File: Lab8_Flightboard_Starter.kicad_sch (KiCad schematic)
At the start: 64 parts, among them J1 Motor1, J10 ESC3_GND, J11 ESC4_VBAT, J12 ESC4_GND, J2 Motor2, J3 Motor3, J4 Motor4, J5 ESC1_VBAT, J6 ESC1_GND, J7 ESC2_VBAT, J8 ESC2_GND, J9 ESC3_VBAT, Q1 DMP6023LE-13, U1 Teensy4.0, U2 TPS62933, U4 LP5912-3.3DRV, U5 LP5912-3.3DRV, U6 NRF24L01_Breakout, U9 LSM6DSO32_Adafruit

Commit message: Fixed more ground nodes
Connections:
- net GND: no longer U1.47 (GND)
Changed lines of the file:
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@@
 	(wire
 		(pts
-			(xy 52.07 133.35) (xy 54.61 133.35)
-		)
-		(stroke
-			(width 0)
-			(type default)
-		)
-	)
-	(wire
-		(pts
 			(xy 143.51 44.45) (xy 147.32 44.45)
 		)
@@
 	(wire
 		(pts
-			(xy 110.49 151.13) (xy 114.3 151.13)
-		)
-		(stroke
-			(width 0)
-			(type default)
-		)
-	)
-	(wire
-		(pts
 			(xy 78.74 53.34) (xy 78.74 52.07)
 		)
@@
 		)
 	)
-	(wire
-		(pts
-			(xy 50.8 173.99) (xy 54.61 173.99)
-		)
-		(stroke
-			(width 0)
-			(type default)
-		)
-	)
 	(polyline
 		(pts
@@
 		)
 	)
-	(label "GND"
-		(at 114.3 151.13 0)
-		(effects
-			(font
-				(size 0.889 0.889)
-			)
-			(justify left bottom)
-		)
-	)
 	(label "SCK"
 		(at 342.9 44.45 180)
@@
 		)
 	)
-	(label "GND"
-		(at 52.07 133.35 180)
-		(effects
-			(font
-				(size 0.889 0.889)
-			)
-			(justify right bottom)
-		)
-	)
-	(label "GND"
-		(at 50.8 173.99 180)
-		(effects
-			(font
-				(size 0.889 0.889)
-			)
-			(justify right bottom)
-		)
-	)
 	(label "CS"
 		(at 278.13 104.14 180)
@@
 	)
 	(symbol
+		(lib_id "power:GND")
+		(at 54.61 173.99 270)
+		(unit 1)
+		(body_style 1)
+		(exclude_from_sim no)
+		(in_bom yes)
+		(on_board yes)
+		(in_pos_files yes)
+		(dnp no)
+		(fields_autoplaced yes)
+		(property "Reference" "#PWR043"
+			(at 48.26 173.99 0)
+			(hide yes)
+			(show_name no)
+			(do_not_autoplace no)
+			(effects
+				(font
+					(size 1.27 1.27)
+				)
+			)
+		)
+		(property "Value" "GND"
+			(at 50.8 173.9899 90)
+			(show_name no)
+			(do_not_autoplace no)
+			(effects
+				(font
+					(size 1.27 1.27)
+				)
+				(justify right)
+			)
+		)
+		(property "Footprint" ""
+			(at 54.61 173.99 0)
+			(hide yes)
+			(show_name no)
+			(do_not_autoplace no)
+			(effects
+				(font
+					(size 1.27 1.27)
+				)
+			)
+		)
+		(property "Datasheet" ""
+			(at 54.61 173.99 0)
+			(hide yes)
+			(show_name no)
+			(do_not_autoplace no)
+			(effects
+				(font
+					(size 1.27 1.27)
+				)
+			)
+		)
+		(property "Description" "Power symbol creates a global label with name \"GND\" , ground"
+			(at 54.61 173.99 0)
+			(hide yes)
+			(show_name no)
+			(do_not_autoplace no)
+			(effects
+				(font
+					(size 1.27 1.27)
+				)
+			)
+		)
+		(pin "1"
+		)
+		(instances
+			(project "Lab8_Flightboard_Starter"
+				(path "/8da9c326-3337-46e2-8624-067ffceed853"
+					(reference "#PWR043")
+					(unit 1)
+				)
+			)
+		)
+	)
+	(symbol
 		(lib_id "IMU_Symbols:LSM6DSO32_Adafruit")
 		(at 293.37 106.68 0)
@@
 	)
 	(symbol
+		(lib_id "power:GND")
+		(at 54.61 133.35 270)
+		(unit 1)
+		(body_style 1)
+		(exclude_from_sim no)
+		(in_bom yes)
+		(on_board yes)
+		(in_pos_files yes)
+		(dnp no)
+		(fields_autoplaced yes)
+		(property "Reference" "#PWR044"
+			(at 48.26 133.35 0)
+			(hide yes)
+			(show_name no)
+			(do_not_autoplace no)
+			(effects
+				(font
+					(size 1.27 1.27)
+				)
+			)
+		)
+		(property "Value" "GND"
+			(at 50.8 133.3499 90)
+			(show_name no)
+			(do_not_autoplace no)
+			(effects
+				(font
+					(size 1.27 1.27)
+				)
+				(justify right)
+			)
+		)
+		(property "Footprint" ""
+			(at 54.61 133.35 0)
+			(hide yes)
+			(show_name no)
+			(do_not_autoplace no)
+			(effects
+				(font
+					(size 1.27 1.27)
+				)
+			)
+		)
+		(property "Datasheet" ""
+			(at 54.61 133.35 0)
+			(hide yes)
+			(show_name no)
+			(do_not_autoplace no)
+			(effects
+				(font
+					(size 1.27 1.27)
+				)
+			)
+		)
+		(property "Description" "Power symbol creates a global label with name \"GND\" , ground"
+			(at 54.61 133.35 0)
+			(hide yes)
+			(show_name no)
+			(do_not_autoplace no)
+			(effects
+				(font
+					(size 1.27 1.27)
+				)
+			)
+		)
+		(pin "1"
+		)
+		(instances
+			(project "Lab8_Flightboard_Starter"
+				(path "/8da9c326-3337-46e2-8624-067ffceed853"
+					(reference "#PWR044")
+					(unit 1)
+				)
+			)
+		)
+	)
+	(symbol
 		(lib_id "Device:C_Small")
 		(at 129.54 83.82 0)
@@
 		(dnp no)
 		(property "Reference" "U1"
-			(at 111.76 138.43 90)
+			(at 83.058 126.746 0)
 			(show_name no)
 			(do_not_autoplace no)

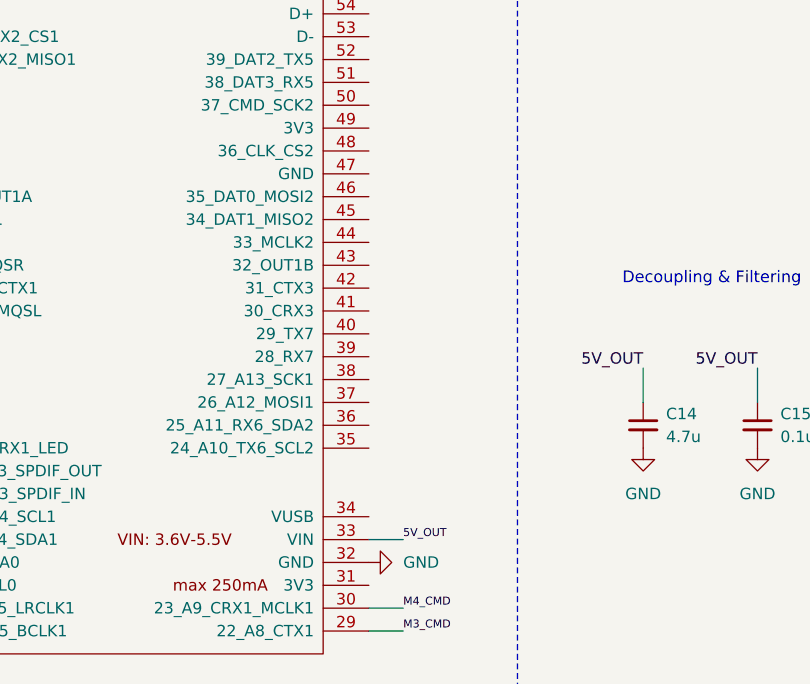
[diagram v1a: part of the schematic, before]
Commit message: Added no connects to MCU
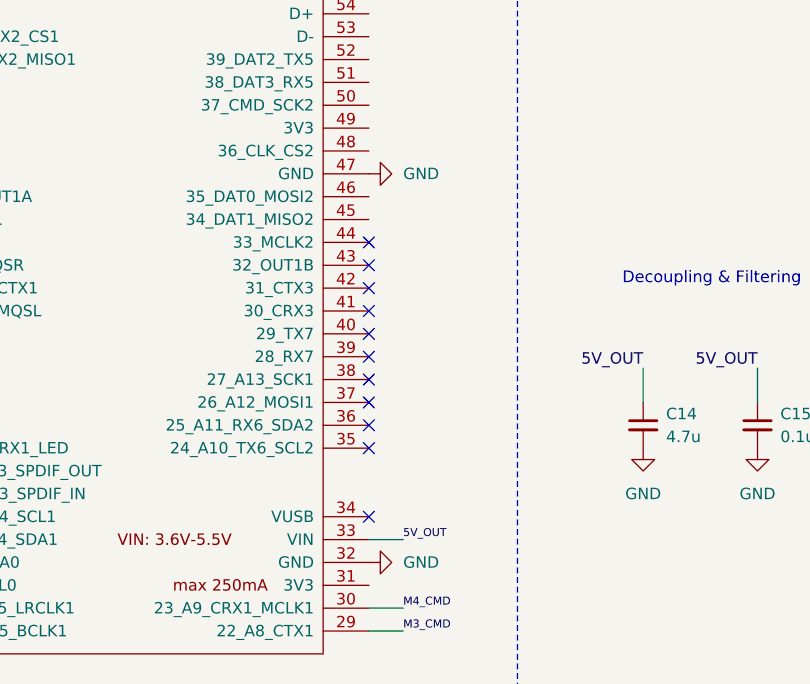
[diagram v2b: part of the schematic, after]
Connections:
- net GND: now also U1.47 (GND)
- no-connect marks 12 -> 23
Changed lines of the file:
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@@
 	)
 	(no_connect
+		(at 110.49 158.75)
+	)
+	(no_connect
 		(at 114.3 83.82)
 	)
 	(no_connect
+		(at 110.49 189.23)
+	)
+	(no_connect
 		(at 308.61 111.76)
 	)
 	(no_connect
+		(at 110.49 166.37)
+	)
+	(no_connect
+		(at 110.49 173.99)
+	)
+	(no_connect
+		(at 110.49 163.83)
+	)
+	(no_connect
 		(at 281.94 109.22)
 	)
@@
 	)
 	(no_connect
+		(at 110.49 171.45)
+	)
+	(no_connect
 		(at 330.2 173.99)
 	)
@@
 	)
 	(no_connect
+		(at 110.49 176.53)
+	)
+	(no_connect
 		(at 295.91 120.65)
 	)
 	(no_connect
+		(at 110.49 179.07)
+	)
+	(no_connect
 		(at 196.85 48.26)
 	)
 	(no_connect
+		(at 110.49 161.29)
+	)
+	(no_connect
 		(at 330.2 185.42)
 	)
@@
 		(at 281.94 111.76)
 	)
+	(no_connect
+		(at 110.49 168.91)
+	)
+	(no_connect
+		(at 110.49 181.61)
+	)
 	(wire
 		(pts
@@
 					(unit 1)
 				)
+			)
+		)
+	)
+	(symbol
+		(lib_id "power:GND")
+		(at 110.49 151.13 90)
+		(unit 1)
+		(body_style 1)
+		(exclude_from_sim no)
+		(in_bom yes)
+		(on_board yes)
+		(in_pos_files yes)
+		(dnp no)
+		(fields_autoplaced yes)
+		(property "Reference" "#PWR045"
+			(at 116.84 151.13 0)
+			(hide yes)
+			(show_name no)
+			(do_not_autoplace no)
+			(effects
+				(font
+					(size 1.27 1.27)
+				)
+			)
+		)
+		(property "Value" "GND"
+			(at 114.3 151.1299 90)
+			(show_name no)
+			(do_not_autoplace no)
+			(effects
+				(font
+					(size 1.27 1.27)
+				)
+				(justify right)
+			)
+		)
+		(property "Footprint" ""
+			(at 110.49 151.13 0)
+			(hide yes)
+			(show_name no)
+			(do_not_autoplace no)
+			(effects
+				(font
+					(size 1.27 1.27)
+				)
+			)
+		)
+		(property "Datasheet" ""
+			(at 110.49 151.13 0)
+			(hide yes)
+			(show_name no)
+			(do_not_autoplace no)
+			(effects
+				(font
+					(size 1.27 1.27)
+				)
+			)
+		)
+		(property "Description" "Power symbol creates a global label with name \"GND\" , ground"
+			(at 110.49 151.13 0)
+			(hide yes)
+			(show_name no)
+			(do_not_autoplace no)
+			(effects
+				(font
+					(size 1.27 1.27)
+				)
+			)
+		)
+		(pin "1"
+		)
+		(instances
+			(project "Lab8_Flightboard_Starter"
+				(path "/8da9c326-3337-46e2-8624-067ffceed853"
+					(reference "#PWR045")
+					(unit 1)
+				)

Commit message: Few design updates
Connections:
- net 3.3V_GP: now also R17.1, TP2.1; no longer R15.1
- net 3.3V_IMU: now also R16.2
- net CS: now also R16.1
- net ADC3: now reaches U1.24 (17_A3_TX4_SDA1)
- net ADC3: now also R15.1
- no-connect marks 23 -> 53
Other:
- moved on the sheet: C24, C25, R16, U1
